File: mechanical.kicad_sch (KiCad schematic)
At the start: 8 parts

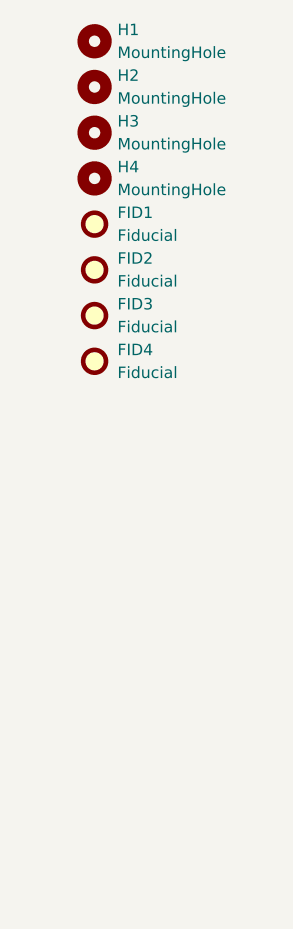
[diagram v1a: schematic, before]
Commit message: feature: add pico debug connections, testpoints
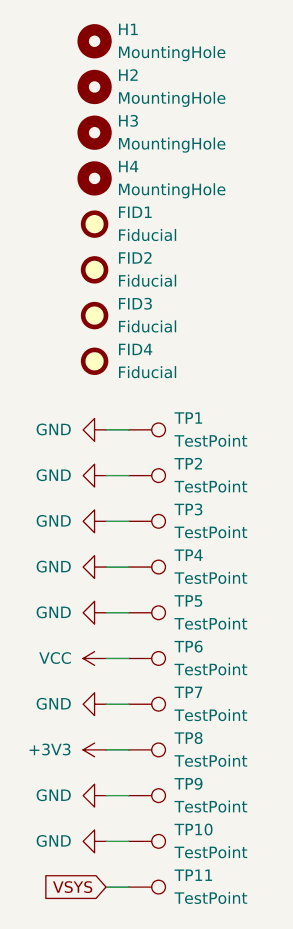
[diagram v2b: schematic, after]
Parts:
- added TP1, TP10, TP11, TP2, TP3, TP4, TP5, TP6, TP7, TP8, TP9: TestPoint, Gigahawk:TestPoint_Keystone_5000-5004_Miniature, symbol Connector:TestPoint
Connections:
- new net +3V3: TP8.1
- new net GND: TP1.1, TP10.1, TP2.1, TP3.1, TP4.1, TP5.1, TP7.1, TP9.1
- new net VCC: TP6.1
- new net VSYS: TP11.1

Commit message: bom: update bom
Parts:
- TP1, TP10, TP11, TP2, TP3, TP4, TP5, TP6, TP7, TP8, TP9: Digikey (none) -> 36-5000-ND
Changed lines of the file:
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@@
+      (effects (font (size 1.27 1.27)) hide)
+    )
+    (property "Digikey" "36-5000-ND" (at 55.88 129.54 0)
       (effects (font (size 1.27 1.27)) hide)
     )
@@
     )
     (property "Datasheet" "~" (at 55.88 99.06 0)
+      (effects (font (size 1.27 1.27)) hide)
+    )
+    (property "Digikey" "36-5000-ND" (at 55.88 93.98 0)
       (effects (font (size 1.27 1.27)) hide)
     )
@@
       (effects (font (size 1.27 1.27)) hide)
     )
+    (property "Digikey" "36-5000-ND" (at 55.88 104.14 0)
+      (effects (font (size 1.27 1.27)) hide)
+    )
     (pin "1")
     (instances
@@
       (effects (font (size 1.27 1.27)) hide)
     )
+    (property "Digikey" "36-5000-ND" (at 55.88 119.38 0)
+      (effects (font (size 1.27 1.27)) hide)
+    )
     (pin "1")
     (instances
@@
     )
     (property "Datasheet" "~" (at 55.88 93.98 0)
+      (effects (font (size 1.27 1.27)) hide)
+    )
+    (property "Digikey" "36-5000-ND" (at 55.88 88.9 0)
       (effects (font (size 1.27 1.27)) hide)
     )
@@
       (effects (font (size 1.27 1.27)) hide)
     )
+    (property "Digikey" "36-5000-ND" (at 55.88 139.7 0)
+      (effects (font (size 1.27 1.27)) hide)
+    )
     (pin "1")
     (instances
@@
       (effects (font (size 1.27 1.27)) hide)
     )
+    (property "Digikey" "36-5000-ND" (at 55.88 134.62 0)
+      (effects (font (size 1.27 1.27)) hide)
+    )
     (pin "1")
     (instances
@@
       (effects (font (size 1.27 1.27)) hide)
     )
+    (property "Digikey" "36-5000-ND" (at 55.88 99.06 0)
+      (effects (font (size 1.27 1.27)) hide)
+    )
     (pin "1")
     (instances
@@
     )
     (property "Datasheet" "~" (at 55.88 129.54 0)
+      (effects (font (size 1.27 1.27)) hide)
+    )
+    (property "Digikey" "36-5000-ND" (at 55.88 124.46 0)
       (effects (font (size 1.27 1.27)) hide)
     )
@@
       (effects (font (size 1.27 1.27)) hide)
     )
+    (property "Digikey" "36-5000-ND" (at 55.88 109.22 0)
+      (effects (font (size 1.27 1.27)) hide)
+    )
     (pin "1")
     (instances
@@
       (effects (font (size 1.27 1.27)) hide)
     )
+    (property "Digikey" "36-5000-ND" (at 55.88 114.3 0)
+      (effects (font (size 1.27 1.27)) hide)
+    )

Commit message: schem: export revision info to all sheets
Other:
- title: (none) -> RepRapDiscount.com Smart Controller
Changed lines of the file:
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@@
 (kicad_sch (version 20230121) (generator eeschema)
-  (paper "A4")
+  (paper "A")
+  (title_block
+    (title "RepRapDiscount.com Smart Controller")
+    (date "${DATE}")
+    (rev "${TAG} (${HASH})")
+  )
   (wire (pts (xy 53.34 114.3) (xy 55.88 114.3))
     (stroke (width 0) (type default))
